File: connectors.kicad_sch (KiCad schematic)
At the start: 29 parts, among them J1 Conn_01x40, J2 Conn_01x09, J6 Conn_Coaxial_Power, SW2 SW_Push

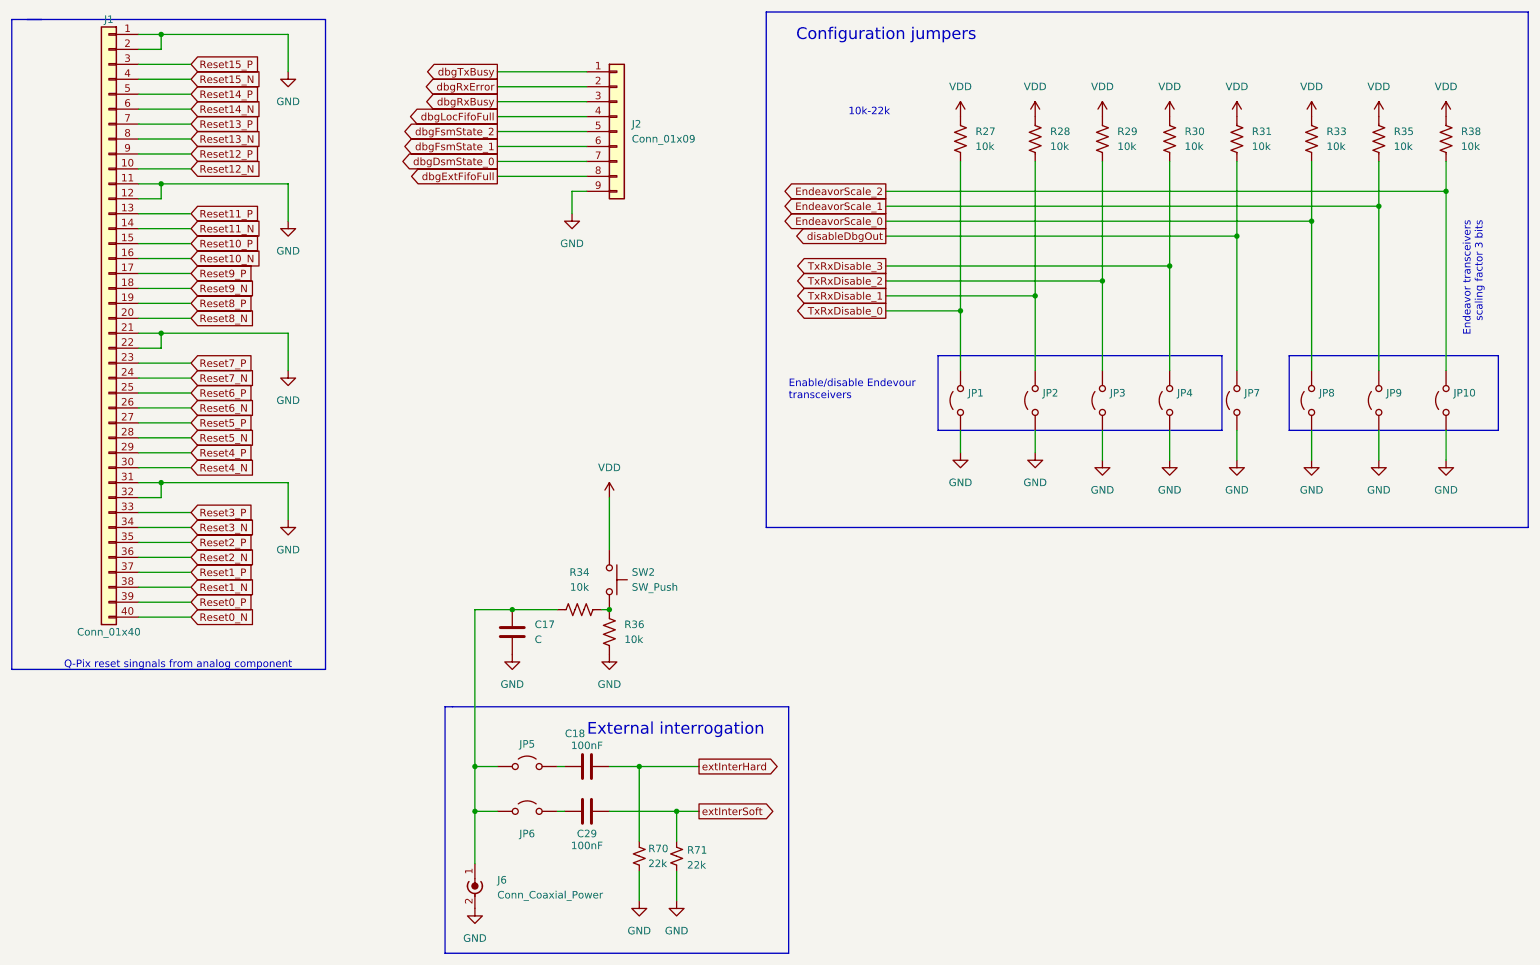
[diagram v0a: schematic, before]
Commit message: add mounting holes, make the board and the zones of rectangular shape, add sikscreen text
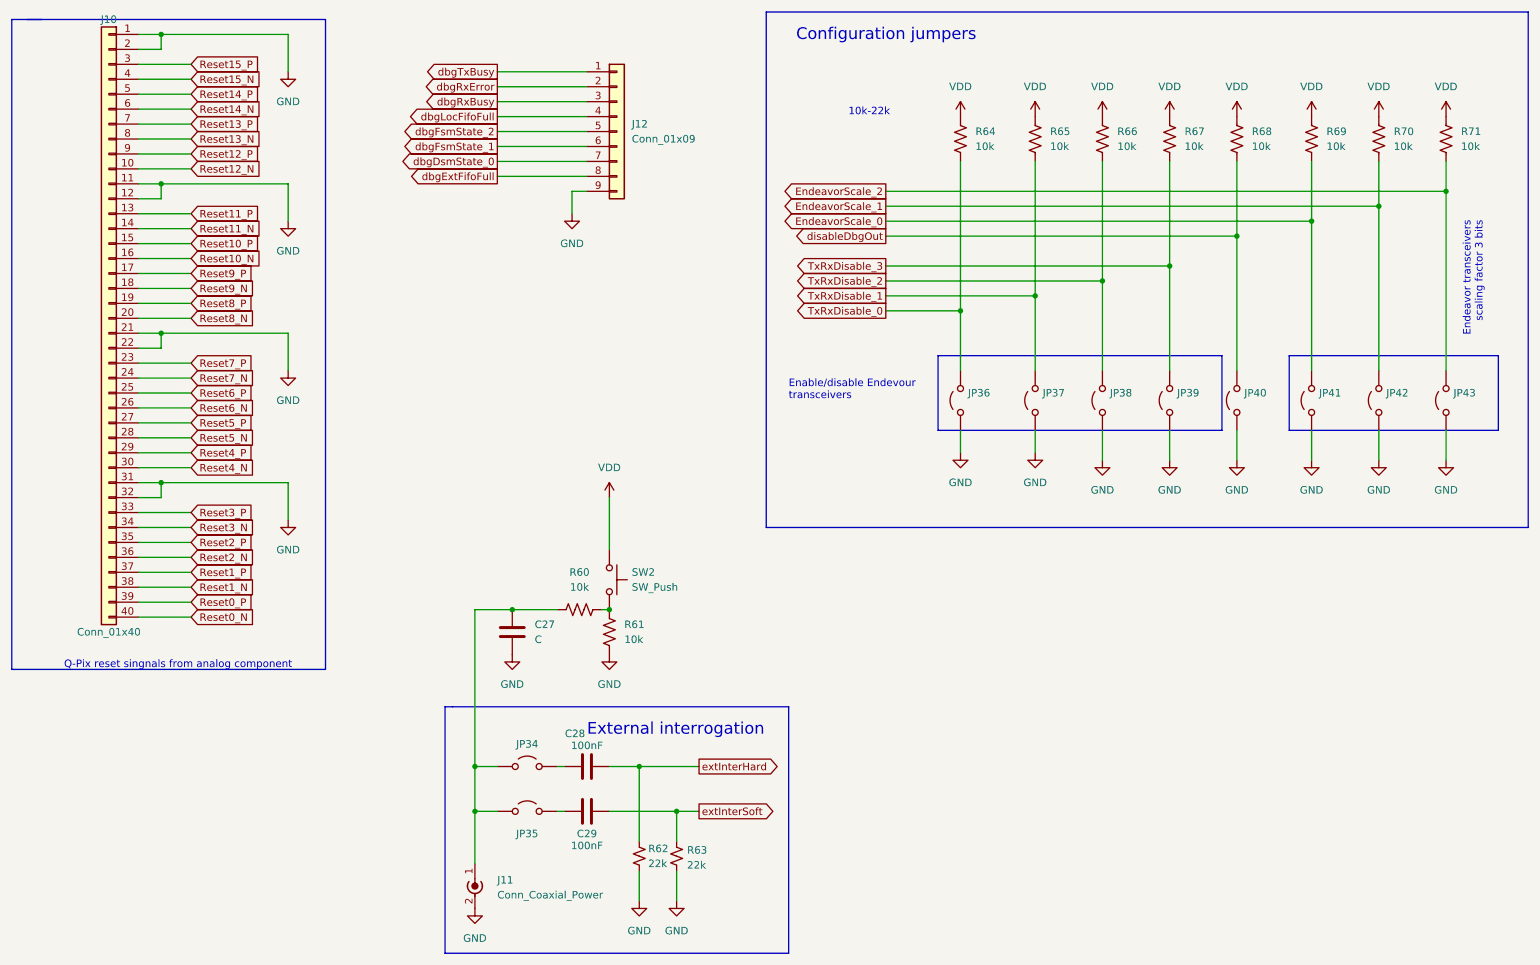
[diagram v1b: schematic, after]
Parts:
- JP34: renamed from JP5; value (none) -> ~
- JP35: renamed from JP6; value (none) -> ~
- JP36: renamed from JP1; value (none) -> ~
- JP37: renamed from JP2; value (none) -> ~
- JP38: renamed from JP3; value (none) -> ~
- JP39: renamed from JP4; value (none) -> ~
- JP40: renamed from JP7; value (none) -> ~
- JP41: renamed from JP8; value (none) -> ~
- JP42: renamed from JP9; value (none) -> ~
- JP43: renamed from JP10; value (none) -> ~
- renumbered C17 to C27, C18 to C28, J1 to J10, J6 to J11, J2 to J12, R34 to R60, R36 to R61, R70 to R62, R71 to R63, R27 to R64, R28 to R65, R29 to R66, R30 to R67, R31 to R68, R33 to R69, R35 to R70, R38 to R71
